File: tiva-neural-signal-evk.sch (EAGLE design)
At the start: 32 parts, among them IC1 TM4C123G, IC2 TLV70233, X1 USB, Y1 16MHz, Y2 32.768kHz

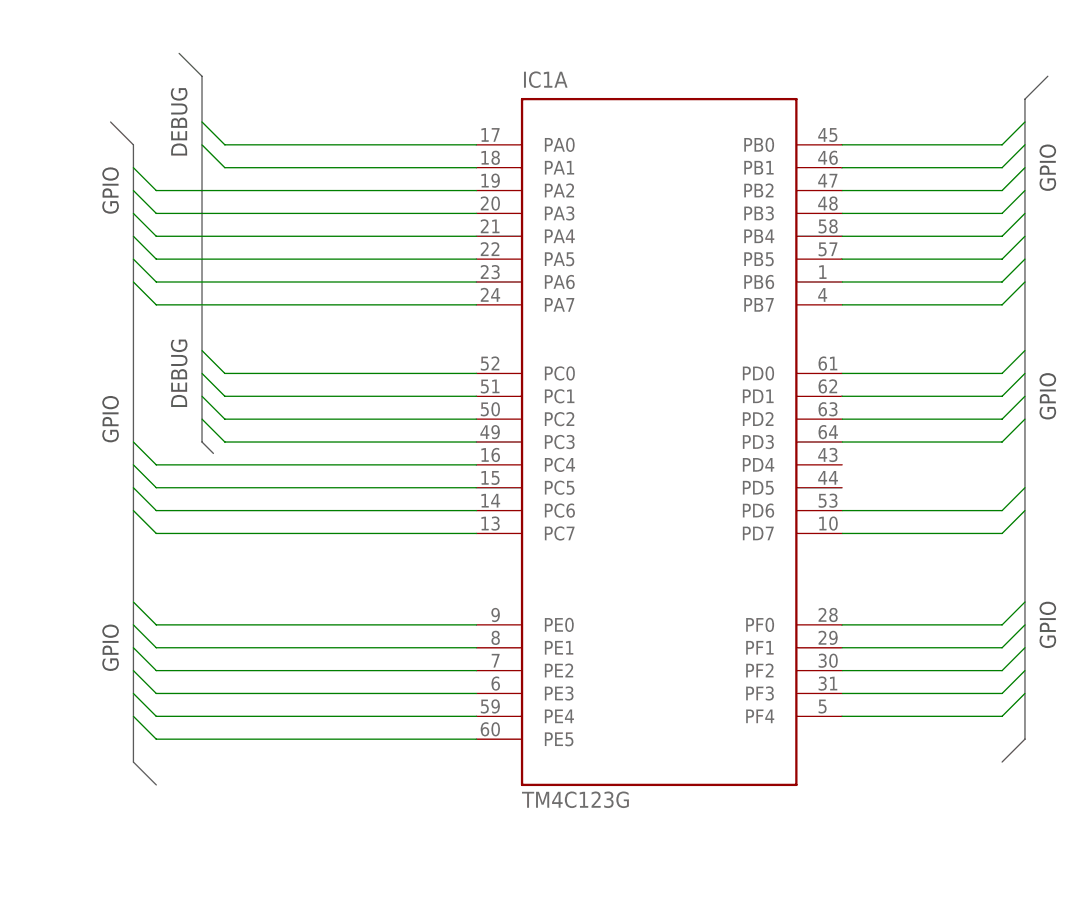
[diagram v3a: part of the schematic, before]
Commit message: added mcu pin names and debug
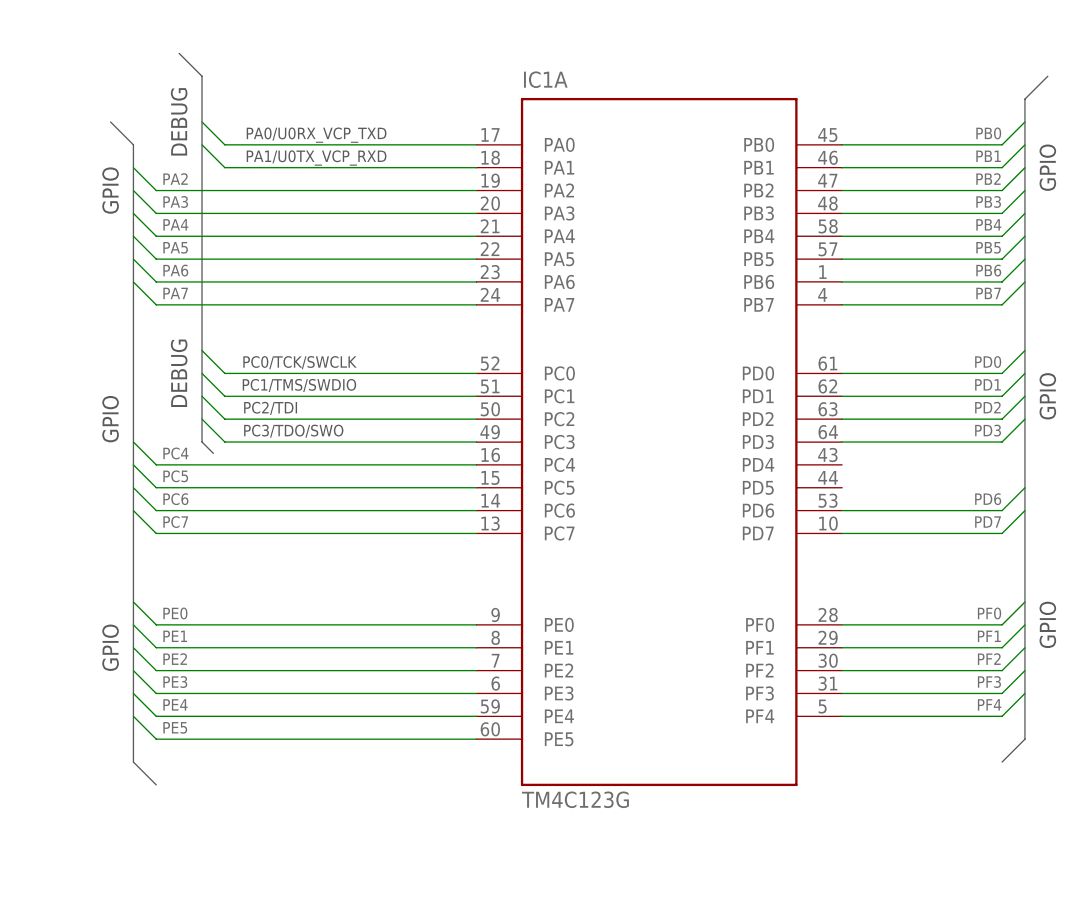
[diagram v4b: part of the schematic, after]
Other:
- note added: "PA0/U0RX_VCP_TXD"
- note added: "PA1/U0TX_VCP_RXD"
- note added: "PC0/TCK/SWCLK"
- note added: "PC1/TMS/SWDIO"
- note added: "PC2/TDI"
- note added: "PC3/TDO/SWO"
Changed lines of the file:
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@@
 <setting verticaltext="up"/>
 </settings>
-<grid distance="0.1" unitdist="inch" unit="inch" style="lines" multiple="1" display="yes" altdistance="0.05" altunitdist="inch" altunit="inch"/>
+<grid distance="0.1" unitdist="inch" unit="inch" style="lines" multiple="1" display="yes" altdistance="0.025" altunitdist="inch" altunit="inch"/>
 <layers>
 <layer number="1" name="Top" color="4" fill="1" visible="no" active="no"/>
@@
 <text x="279.4" y="205.74" size="1.778" layer="97" rot="R90" align="center">DEBUG</text>
 <text x="279.4" y="233.68" size="1.778" layer="97" rot="R90" align="center">DEBUG</text>
+<text x="294.64" y="232.41" size="1.27" layer="97" align="center">PA0/U0RX_VCP_TXD</text>
+<text x="294.64" y="229.87" size="1.27" layer="97" align="center">PA1/U0TX_VCP_RXD</text>
+<text x="292.735" y="207.01" size="1.27" layer="97" align="center">PC0/TCK/SWCLK</text>
+<text x="292.735" y="204.47" size="1.27" layer="97" align="center">PC1/TMS/SWDIO</text>
+<text x="289.56" y="201.93" size="1.27" layer="97" align="center">PC2/TDI</text>
+<text x="292.1" y="199.39" size="1.27" layer="97" align="center">PC3/TDO/SWO</text>
 </plain>
 <instances>
@@
 <wire x1="312.42" y1="226.06" x2="276.86" y2="226.06" width="0.1524" layer="91"/>
 <wire x1="276.86" y1="226.06" x2="274.32" y2="228.6" width="0.1524" layer="91"/>
+<label x="277.495" y="226.695" size="1.27" layer="95"/>
 </segment>
 </net>
@@
 <wire x1="312.42" y1="223.52" x2="276.86" y2="223.52" width="0.1524" layer="91"/>
 <wire x1="276.86" y1="223.52" x2="274.32" y2="226.06" width="0.1524" layer="91"/>
+<label x="277.495" y="224.155" size="1.27" layer="95"/>
 </segment>
 </net>
@@
 <wire x1="312.42" y1="220.98" x2="276.86" y2="220.98" width="0.1524" layer="91"/>
 <wire x1="276.86" y1="220.98" x2="274.32" y2="223.52" width="0.1524" layer="91"/>
+<label x="277.495" y="221.615" size="1.27" layer="95"/>
 </segment>
 </net>
@@
 <wire x1="312.42" y1="218.44" x2="276.86" y2="218.44" width="0.1524" layer="91"/>
 <wire x1="276.86" y1="218.44" x2="274.32" y2="220.98" width="0.1524" layer="91"/>
+<label x="277.495" y="219.075" size="1.27" layer="95"/>
 </segment>
 </net>
@@
 <wire x1="312.42" y1="215.9" x2="276.86" y2="215.9" width="0.1524" layer="91"/>
 <wire x1="276.86" y1="215.9" x2="274.32" y2="218.44" width="0.1524" layer="91"/>
+<label x="277.495" y="216.535" size="1.27" layer="95"/>
 </segment>
 </net>
@@
 <wire x1="312.42" y1="213.36" x2="276.86" y2="213.36" width="0.1524" layer="91"/>
 <wire x1="276.86" y1="213.36" x2="274.32" y2="215.9" width="0.1524" layer="91"/>
+<label x="277.495" y="213.995" size="1.27" layer="95"/>
 </segment>
 </net>
@@
 <wire x1="312.42" y1="195.58" x2="276.86" y2="195.58" width="0.1524" layer="91"/>
 <wire x1="276.86" y1="195.58" x2="274.32" y2="198.12" width="0.1524" layer="91"/>
+<label x="277.495" y="196.215" size="1.27" layer="95"/>
 </segment>
 </net>
@@
 <wire x1="312.42" y1="193.04" x2="276.86" y2="193.04" width="0.1524" layer="91"/>
 <wire x1="276.86" y1="193.04" x2="274.32" y2="195.58" width="0.1524" layer="91"/>
+<label x="277.495" y="193.675" size="1.27" layer="95"/>
 </segment>
 </net>
@@
 <wire x1="312.42" y1="190.5" x2="276.86" y2="190.5" width="0.1524" layer="91"/>
 <wire x1="276.86" y1="190.5" x2="274.32" y2="193.04" width="0.1524" layer="91"/>
+<label x="277.495" y="191.135" size="1.27" layer="95"/>
 </segment>
 </net>
@@
 <wire x1="312.42" y1="187.96" x2="276.86" y2="187.96" width="0.1524" layer="91"/>
 <wire x1="276.86" y1="187.96" x2="274.32" y2="190.5" width="0.1524" layer="91"/>
+<label x="277.495" y="188.595" size="1.27" layer="95"/>
 </segment>
 </net>
@@
 <wire x1="312.42" y1="177.8" x2="276.86" y2="177.8" width="0.1524" layer="91"/>
 <wire x1="276.86" y1="177.8" x2="274.32" y2="180.34" width="0.1524" layer="91"/>
+<label x="277.495" y="178.435" size="1.27" layer="95"/>
 </segment>
 </net>
@@
 <wire x1="312.42" y1="175.26" x2="276.86" y2="175.26" width="0.1524" layer="91"/>
 <wire x1="276.86" y1="175.26" x2="274.32" y2="177.8" width="0.1524" layer="91"/>
+<label x="277.495" y="175.895" size="1.27" layer="95"/>
 </segment>
 </net>
@@
 <wire x1="312.42" y1="172.72" x2="276.86" y2="172.72" width="0.1524" layer="91"/>
 <wire x1="276.86" y1="172.72" x2="274.32" y2="175.26" width="0.1524" layer="91"/>
+<label x="277.495" y="173.355" size="1.27" layer="95"/>
 </segment>
 </net>
@@
 <wire x1="312.42" y1="170.18" x2="276.86" y2="170.18" width="0.1524" layer="91"/>
 <wire x1="276.86" y1="170.18" x2="274.32" y2="172.72" width="0.1524" layer="91"/>
+<label x="277.495" y="170.815" size="1.27" layer="95"/>
 </segment>
 </net>
@@
 <wire x1="312.42" y1="167.64" x2="276.86" y2="167.64" width="0.1524" layer="91"/>
 <wire x1="276.86" y1="167.64" x2="274.32" y2="170.18" width="0.1524" layer="91"/>
+<label x="277.495" y="168.275" size="1.27" layer="95"/>
 </segment>
 </net>
@@
 <wire x1="312.42" y1="165.1" x2="276.86" y2="165.1" width="0.1524" layer="91"/>
 <wire x1="276.86" y1="165.1" x2="274.32" y2="167.64" width="0.1524" layer="91"/>
+<label x="277.495" y="165.735" size="1.27" layer="95"/>
 </segment>
 </net>
@@
 <wire x1="353.06" y1="231.14" x2="370.84" y2="231.14" width="0.1524" layer="91"/>
 <wire x1="370.84" y1="231.14" x2="373.38" y2="233.68" width="0.1524" layer="91"/>
+<label x="370.84" y="233.045" size="1.27" layer="95" rot="R180"/>
 </segment>
 </net>
@@
 <wire x1="353.06" y1="228.6" x2="370.84" y2="228.6" width="0.1524" layer="91"/>
 <wire x1="370.84" y1="228.6" x2="373.38" y2="231.14" width="0.1524" layer="91"/>
+<label x="370.84" y="230.505" size="1.27" layer="95" rot="R180"/>
 </segment>
 </net>
@@
 <wire x1="353.06" y1="226.06" x2="370.84" y2="226.06" width="0.1524" layer="91"/>
 <wire x1="370.84" y1="226.06" x2="373.38" y2="228.6" width="0.1524" layer="91"/>
+<label x="370.84" y="227.965" size="1.27" layer="95" rot="R180"/>
 </segment>
 </net>
@@
 <wire x1="353.06" y1="223.52" x2="370.84" y2="223.52" width="0.1524" layer="91"/>
 <wire x1="370.84" y1="223.52" x2="373.38" y2="226.06" width="0.1524" layer="91"/>
+<label x="370.84" y="225.425" size="1.27" layer="95" rot="R180"/>
 </segment>
 </net>
@@
 <wire x1="353.06" y1="220.98" x2="370.84" y2="220.98" width="0.1524" layer="91"/>
 <wire x1="370.84" y1="220.98" x2="373.38" y2="223.52" width="0.1524" layer="91"/>
+<label x="370.84" y="222.885" size="1.27" layer="95" rot="R180"/>
 </segment>
 </net>
@@
 <wire x1="353.06" y1="218.44" x2="370.84" y2="218.44" width="0.1524" layer="91"/>
 <wire x1="370.84" y1="218.44" x2="373.38" y2="220.98" width="0.1524" layer="91"/>
+<label x="370.84" y="220.345" size="1.27" layer="95" rot="R180"/>
 </segment>
 </net>
@@
 <wire x1="353.06" y1="215.9" x2="370.84" y2="215.9" width="0.1524" layer="91"/>
 <wire x1="370.84" y1="215.9" x2="373.38" y2="218.44" width="0.1524" layer="91"/>
+<label x="370.84" y="217.805" size="1.27" layer="95" rot="R180"/>
 </segment>
 </net>
@@
 <wire x1="353.06" y1="213.36" x2="370.84" y2="213.36" width="0.1524" layer="91"/>
 <wire x1="370.84" y1="213.36" x2="373.38" y2="215.9" width="0.1524" layer="91"/>
+<label x="370.84" y="215.265" size="1.27" layer="95" rot="R180"/>
 </segment>
 </net>
@@
 <wire x1="353.06" y1="205.74" x2="370.84" y2="205.74" width="0.1524" layer="91"/>
 <wire x1="370.84" y1="205.74" x2="373.38" y2="208.28" width="0.1524" layer="91"/>
+<label x="370.84" y="207.645" size="1.27" layer="95" rot="R180"/>
 </segment>
 </net>
@@
 <wire x1="353.06" y1="203.2" x2="370.84" y2="203.2" width="0.1524" layer="91"/>
 <wire x1="370.84" y1="203.2" x2="373.38" y2="205.74" width="0.1524" layer="91"/>
+<label x="370.84" y="205.105" size="1.27" layer="95" rot="R180"/>
 </segment>
 </net>
@@
 <wire x1="353.06" y1="200.66" x2="370.84" y2="200.66" width="0.1524" layer="91"/>
 <wire x1="370.84" y1="200.66" x2="373.38" y2="203.2" width="0.1524" layer="91"/>
+<label x="370.84" y="202.565" size="1.27" layer="95" rot="R180"/>
 </segment>
 </net>
@@
 <wire x1="353.06" y1="198.12" x2="370.84" y2="198.12" width="0.1524" layer="91"/>
 <wire x1="370.84" y1="198.12" x2="373.38" y2="200.66" width="0.1524" layer="91"/>
+<label x="370.84" y="200.025" size="1.27" layer="95" rot="R180"/>
 </segment>
 </net>
@@
 <wire x1="353.06" y1="190.5" x2="370.84" y2="190.5" width="0.1524" layer="91"/>
 <wire x1="370.84" y1="190.5" x2="373.38" y2="193.04" width="0.1524" layer="91"/>
+<label x="370.84" y="192.405" size="1.27" layer="95" rot="R180"/>
 </segment>
 </net>
@@
 <wire x1="353.06" y1="187.96" x2="370.84" y2="187.96" width="0.1524" layer="91"/>
 <wire x1="370.84" y1="187.96" x2="373.38" y2="190.5" width="0.1524" layer="91"/>
+<label x="370.84" y="189.865" size="1.27" layer="95" rot="R180"/>
 </segment>
 </net>
@@
 <wire x1="353.06" y1="177.8" x2="370.84" y2="177.8" width="0.1524" layer="91"/>
 <wire x1="370.84" y1="177.8" x2="373.38" y2="180.34" width="0.1524" layer="91"/>
+<label x="370.84" y="179.705" size="1.27" layer="95" rot="R180"/>
 </segment>
 </net>
@@
 <wire x1="353.06" y1="175.26" x2="370.84" y2="175.26" width="0.1524" layer="91"/>
 <wire x1="370.84" y1="175.26" x2="373.38" y2="177.8" width="0.1524" layer="91"/>
+<label x="370.84" y="177.165" size="1.27" layer="95" rot="R180"/>
 </segment>
 </net>
@@
 <wire x1="353.06" y1="172.72" x2="370.84" y2="172.72" width="0.1524" layer="91"/>
 <wire x1="370.84" y1="172.72" x2="373.38" y2="175.26" width="0.1524" layer="91"/>
+<label x="370.84" y="174.625" size="1.27" layer="95" rot="R180"/>
 </segment>
 </net>
@@
 <wire x1="353.06" y1="170.18" x2="370.84" y2="170.18" width="0.1524" layer="91"/>
 <wire x1="370.84" y1="170.18" x2="373.38" y2="172.72" width="0.1524" layer="91"/>
+<label x="370.84" y="172.085" size="1.27" layer="95" rot="R180"/>
 </segment>
 </net>
@@
 <wire x1="353.06" y1="167.64" x2="370.84" y2="167.64" width="0.1524" layer="91"/>
 <wire x1="370.84" y1="167.64" x2="373.38" y2="170.18" width="0.1524" layer="91"/>
-</segment>
-</net>
+<label x="370.84" y="169.545" size="1.27" layer="95" rot="R180"/>
+</segment>
+</net>

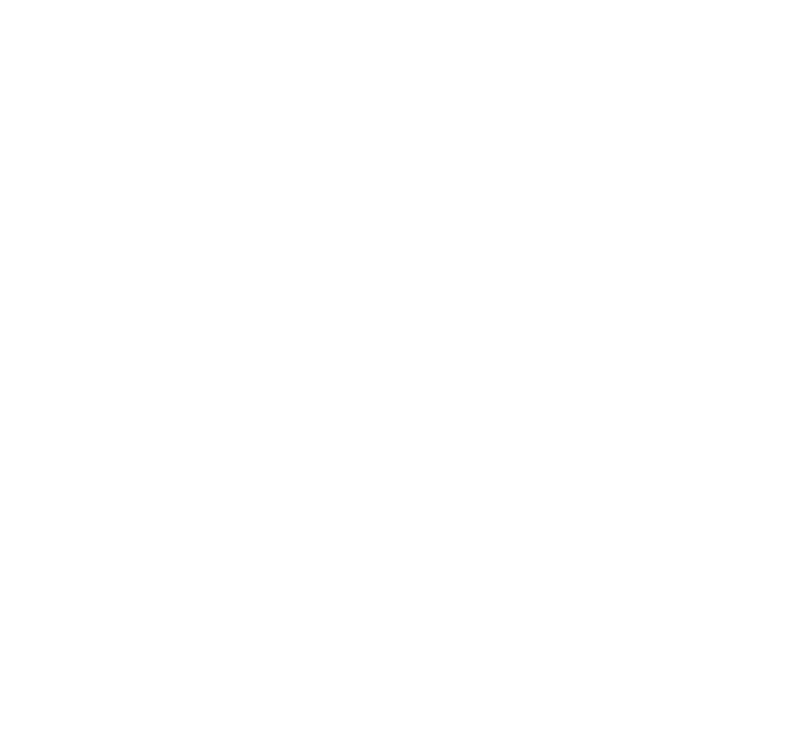
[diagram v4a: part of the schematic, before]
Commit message: added SD card in SPI mode
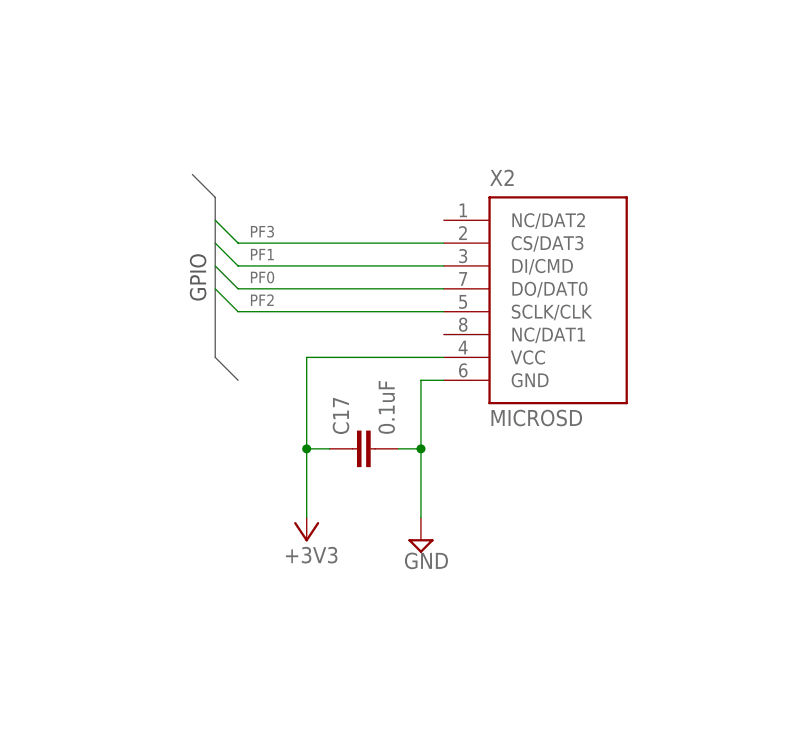
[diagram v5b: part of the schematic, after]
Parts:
- added C17: 0.1uF, rcl:C-EUC0603
- added X2: MICROSD, mor307:MICROSD
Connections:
- net +3V3: now also C17.1, X2.VCC
- net GND: now also C17.2, X2.GND
- net PF0: now also X2.DO/DAT0
- net PF1: now also X2.DI/CMD
- net PF2: now also X2.SCLK/CLK
- net PF3: now also X2.CS/DAT3
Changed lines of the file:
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@@
 <part name="+3V2" library="supply1" deviceset="+3V3" device=""/>
 <part name="RESET" library="testpad" deviceset="TP" device="B1,27"/>
+<part name="X2" library="mor307" deviceset="MICROSD" device=""/>
+<part name="C17" library="rcl" deviceset="C-EU" device="C0603" value="0.1uF"/>
+<part name="SUPPLY12" library="supply2" deviceset="GND" device=""/>
+<part name="+3V4" library="supply1" deviceset="+3V3" device=""/>
 </parts>
 <sheets>
@@
 <text x="289.56" y="201.93" size="1.27" layer="97" align="center">PC2/TDI</text>
 <text x="292.1" y="199.39" size="1.27" layer="97" align="center">PC3/TDO/SWO</text>
+<text x="313.055" y="125.73" size="1.778" layer="97" rot="R90" align="center">GPIO</text>
 </plain>
 <instances>
@@
 <attribute name="TP_SIGNAL_NAME" x="153.67" y="240.03" size="1.778" layer="97"/>
 </instance>
+<instance part="X2" gate="G$1" x="353.06" y="121.92"/>
+<instance part="C17" gate="G$1" x="330.2" y="106.68" rot="R90"/>
+<instance part="SUPPLY12" gate="GND" x="337.82" y="96.52"/>
+<instance part="+3V4" gate="G$1" x="325.12" y="96.52" smashed="yes" rot="R180">
+<attribute name="VALUE" x="322.58" y="93.98" size="1.778" layer="96"/>
+</instance>
 </instances>
 <busses>
@@
 <wire x1="274.32" y1="231.14" x2="274.32" y2="162.56" width="0.762" layer="92"/>
 <wire x1="274.32" y1="162.56" x2="276.86" y2="160.02" width="0.762" layer="92"/>
+</segment>
+<segment>
+<wire x1="312.42" y1="137.16" x2="314.96" y2="134.62" width="0.762" layer="92"/>
+<wire x1="314.96" y1="134.62" x2="314.96" y2="116.84" width="0.762" layer="92"/>
+<wire x1="314.96" y1="116.84" x2="317.5" y2="114.3" width="0.762" layer="92"/>
 </segment>
 </bus>
@@
 <wire x1="129.54" y1="222.25" x2="127" y2="222.25" width="0.1524" layer="91"/>
 <junction x="127" y="222.25"/>
+</segment>
+<segment>
+<pinref part="X2" gate="G$1" pin="GND"/>
+<wire x1="340.36" y1="114.3" x2="337.82" y2="114.3" width="0.1524" layer="91"/>
+<wire x1="337.82" y1="114.3" x2="337.82" y2="106.68" width="0.1524" layer="91"/>
+<pinref part="C17" gate="G$1" pin="2"/>
+<wire x1="337.82" y1="106.68" x2="335.28" y2="106.68" width="0.1524" layer="91"/>
+<pinref part="SUPPLY12" gate="GND" pin="GND"/>
+<wire x1="337.82" y1="106.68" x2="337.82" y2="99.06" width="0.1524" layer="91"/>
+<junction x="337.82" y="106.68"/>
 </segment>
 </net>
@@
 <wire x1="139.7" y1="223.52" x2="139.7" y2="220.98" width="0.1524" layer="91"/>
 </segment>
+<segment>
+<pinref part="X2" gate="G$1" pin="VCC"/>
+<wire x1="340.36" y1="116.84" x2="325.12" y2="116.84" width="0.1524" layer="91"/>
+<wire x1="325.12" y1="116.84" x2="325.12" y2="106.68" width="0.1524" layer="91"/>
+<pinref part="C17" gate="G$1" pin="1"/>
+<wire x1="325.12" y1="106.68" x2="327.66" y2="106.68" width="0.1524" layer="91"/>
+<pinref part="+3V4" gate="G$1" pin="+3V3"/>
+<wire x1="325.12" y1="106.68" x2="325.12" y2="99.06" width="0.1524" layer="91"/>
+<junction x="325.12" y="106.68"/>
+</segment>
 </net>
 <net name="!HIB!" class="0">
@@
 <label x="370.84" y="179.705" size="1.27" layer="95" rot="R180"/>
 </segment>
+<segment>
+<pinref part="X2" gate="G$1" pin="DO/DAT0"/>
+<wire x1="340.36" y1="124.46" x2="317.5" y2="124.46" width="0.1524" layer="91"/>
+<wire x1="317.5" y1="124.46" x2="314.96" y2="127" width="0.1524" layer="91"/>
+<label x="318.77" y="125.095" size="1.27" layer="95"/>
+</segment>
 </net>
 <net name="PF1" class="0">
@@
 <label x="370.84" y="177.165" size="1.27" layer="95" rot="R180"/>
 </segment>
+<segment>
+<pinref part="X2" gate="G$1" pin="DI/CMD"/>
+<wire x1="340.36" y1="127" x2="317.5" y2="127" width="0.1524" layer="91"/>
+<wire x1="317.5" y1="127" x2="314.96" y2="129.54" width="0.1524" layer="91"/>
+<label x="318.77" y="127.635" size="1.27" layer="95"/>
+</segment>
 </net>
 <net name="PF2" class="0">
@@
 <label x="370.84" y="174.625" size="1.27" layer="95" rot="R180"/>
 </segment>
+<segment>
+<pinref part="X2" gate="G$1" pin="SCLK/CLK"/>
+<wire x1="340.36" y1="121.92" x2="317.5" y2="121.92" width="0.1524" layer="91"/>
+<wire x1="317.5" y1="121.92" x2="314.96" y2="124.46" width="0.1524" layer="91"/>
+<label x="318.77" y="122.555" size="1.27" layer="95"/>
+</segment>
 </net>
 <net name="PF3" class="0">
@@
 <label x="370.84" y="172.085" size="1.27" layer="95" rot="R180"/>
 </segment>
-</net>
+<segment>
+<pinref part="X2" gate="G$1" pin="CS/DAT3"/>
+<wire x1="340.36" y1="129.54" x2="317.5" y2="129.54" width="0.1524" layer="91"/>
+<wire x1="317.5" y1="129.54" x2="314.96" y2="132.08" width="0.1524" layer="91"/>
+<label x="318.77" y="130.175" size="1.27" layer="95"/>
+</segment>
+</net>
